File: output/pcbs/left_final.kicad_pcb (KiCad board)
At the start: 2 copper layers, 137 x 129 mm, 79 parts

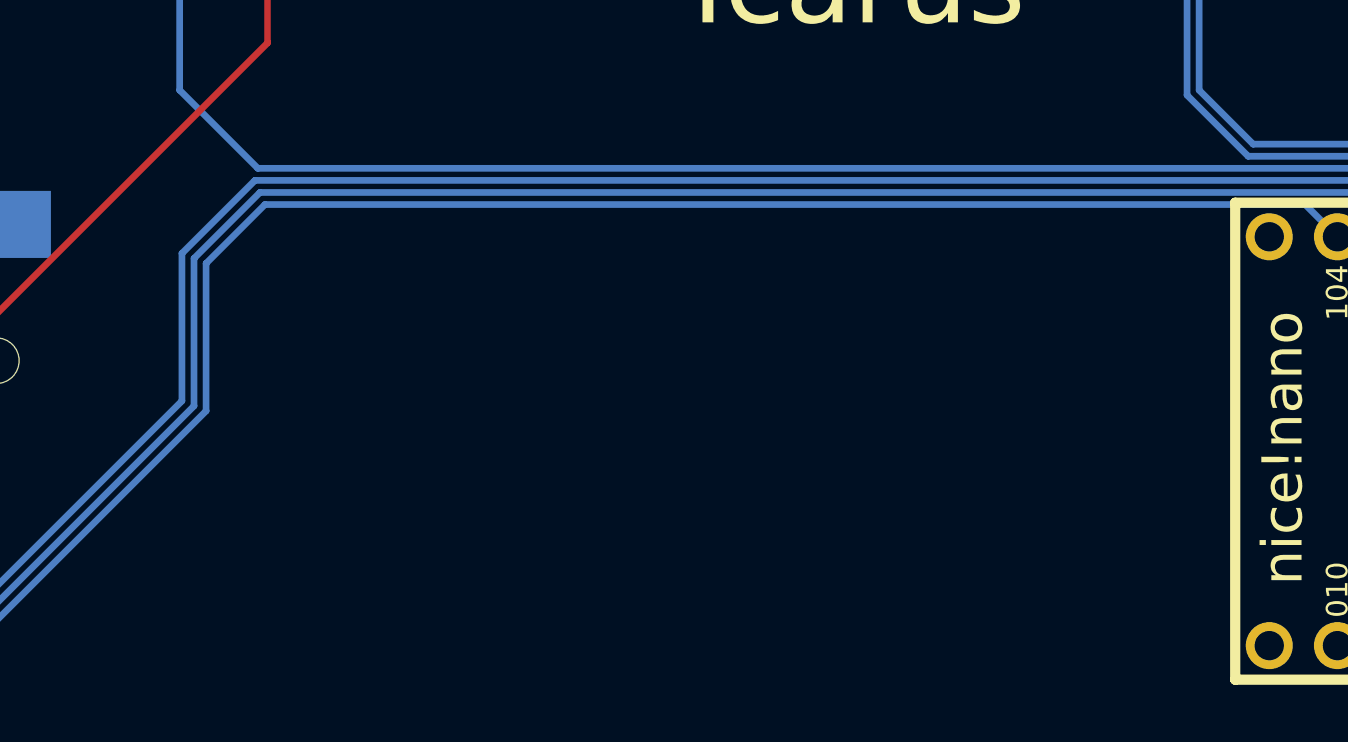
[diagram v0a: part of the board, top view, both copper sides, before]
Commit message: redesign for short board, left but no right pcb. Final pcbs for old design
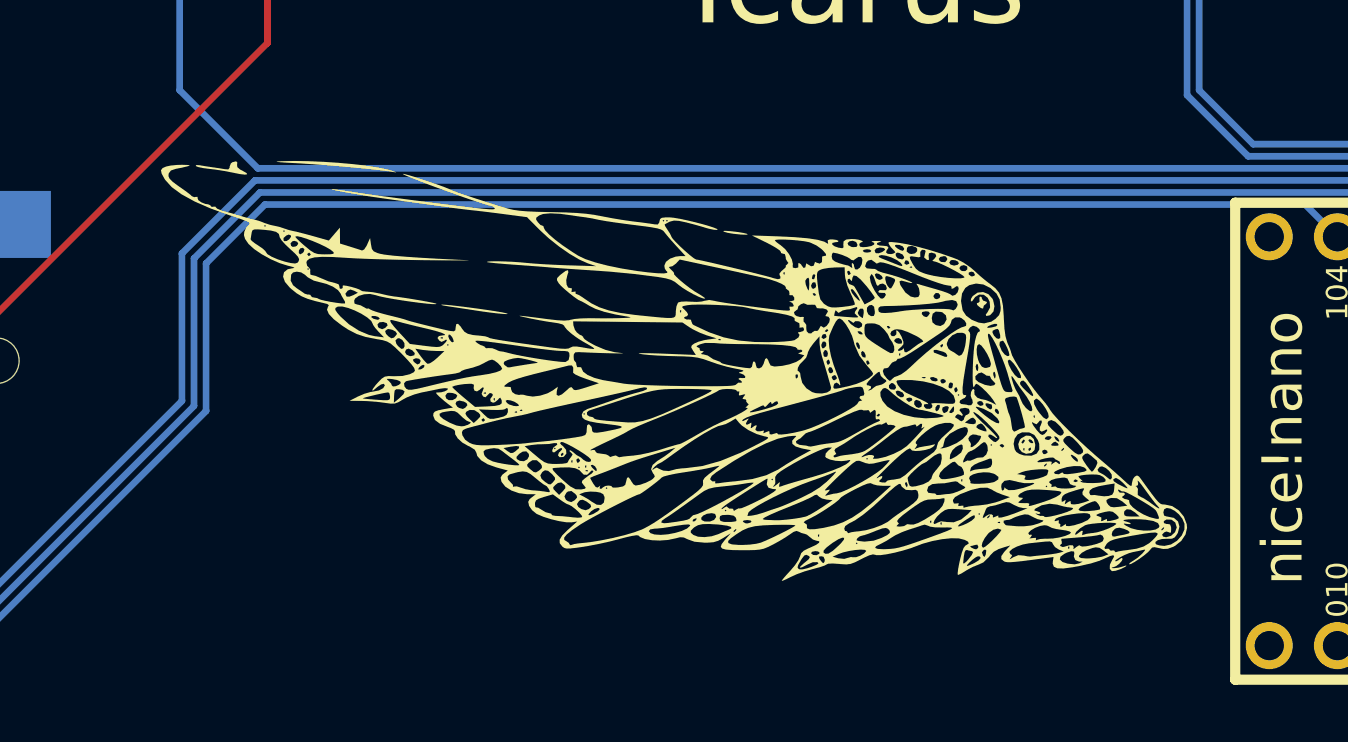
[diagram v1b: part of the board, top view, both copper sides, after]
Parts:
- added G***: LOGO, left_wing, F.Cu at (168.9, 197.1)
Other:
- rule pad_to_mask_clearance: 0.05 -> 0
